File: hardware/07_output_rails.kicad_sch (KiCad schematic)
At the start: 5 parts, among them J2 16-pin IDC POWER OUT, J7 Manual IDC wire landing

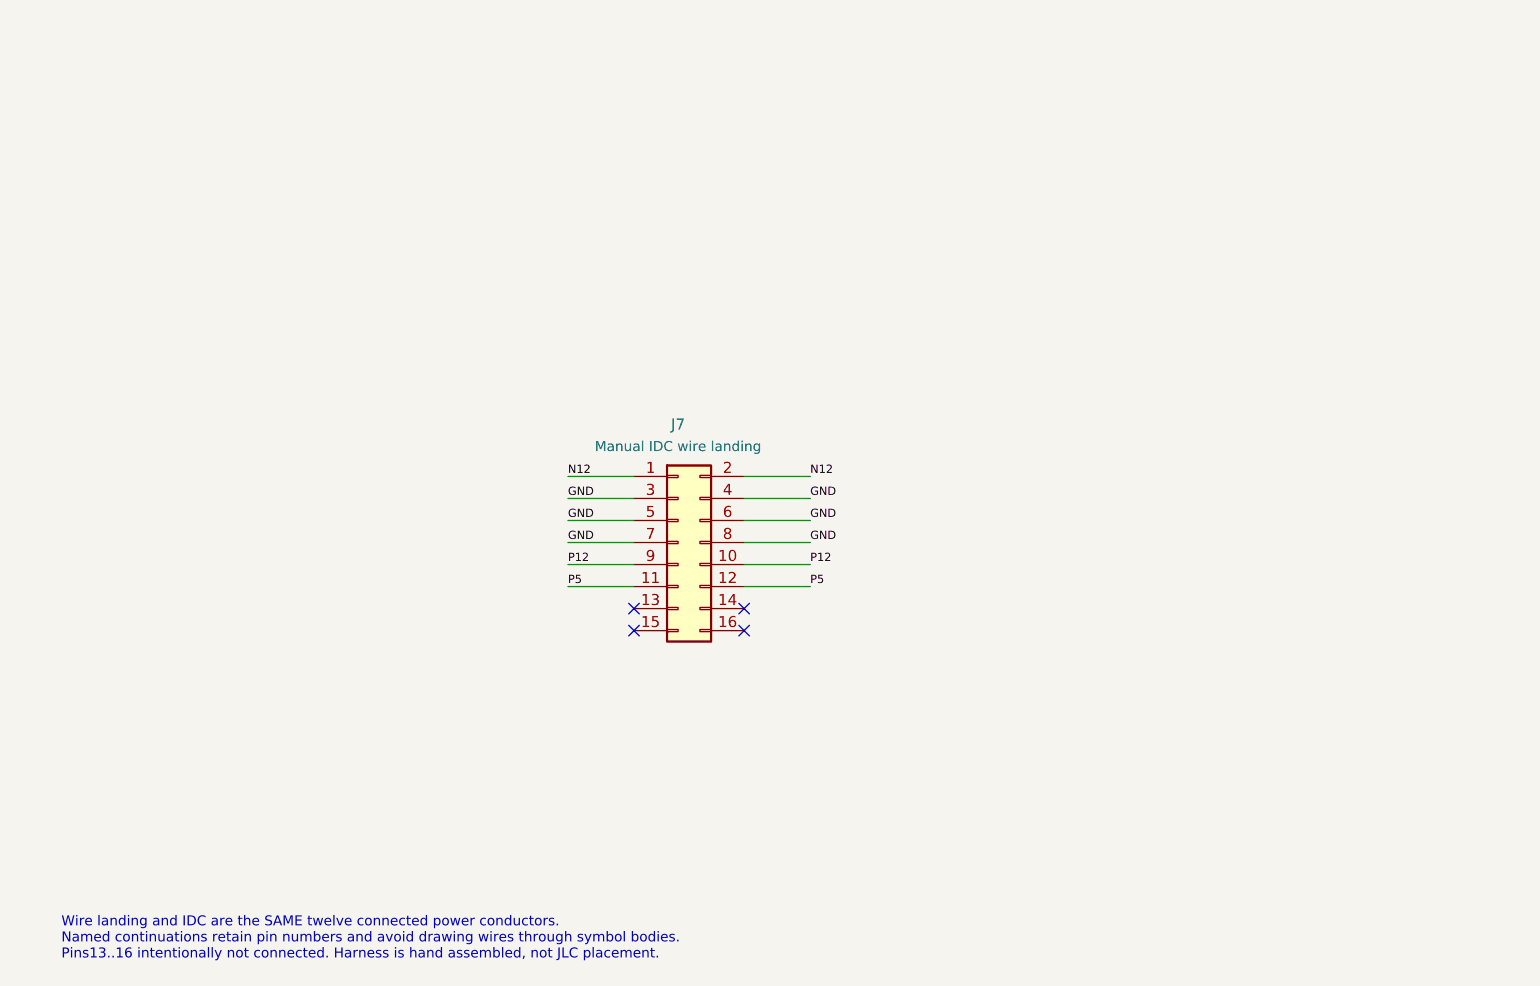
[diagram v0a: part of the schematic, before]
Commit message: Replace MCU diagnostics with optional rail-sense IDC and single 5 V power LED
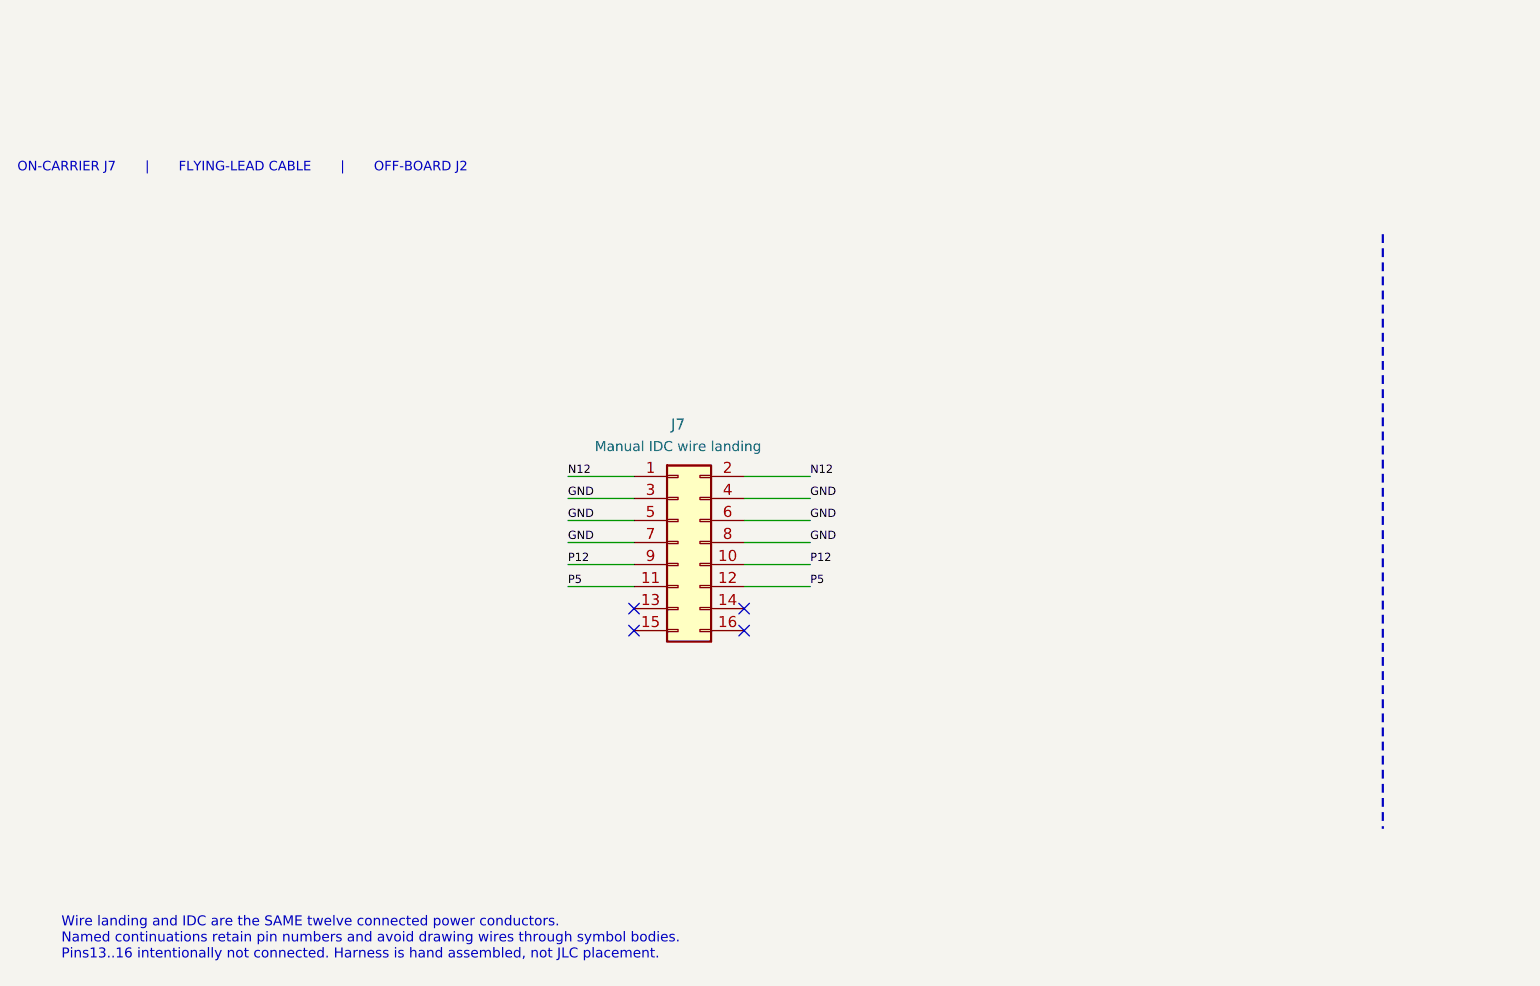
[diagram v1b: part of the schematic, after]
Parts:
- J2: NOTE Off-board cable connector exact MPN open. Manual J7->J2 pin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 -> OFF-BOARD endpoint of ONE J7->J2 flying-lead power harness,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
- J7: NOTE Actual reserved carrier wire landing, not a box header on P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 -> ON-CARRIER numbered solder lands, not an extra purchasable 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
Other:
- note added: "ON-CARRIER J7 | FLYING-LEAD CABLE | OFF-BOARD J2"
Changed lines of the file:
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@@
 (text "07 / MANUAL OUTPUT HARNESS" (at 20.32 17.78 0) (effects (font (size 2.2 2.2)) (justify left)))
 (text "J7 board wire landing -> J2 off-board IDC cable, pin-for-pin.\n1/2=-12, 3..8=GND, 9/10=+12, 11/12=+5; 13..16 NC.\nNever connect another active PSU. Continuity-test red stripe / orientation before use." (at 20.32 30.48 0) (effects (font (size 1.02 1.02)) (justify left)))
+(text "ON-CARRIER J7       |       FLYING-LEAD CABLE       |       OFF-BOARD J2" (at 20.32 60.96 0) (effects (font (size 1.1 1.1)) (justify left)))
+(polyline (pts (xy 177.8 68.58) (xy 177.8 137.16)) (stroke (width 0.254) (type dash)) (fill (type none)))
 (label "N12" (at 83.82 96.52 0) (effects (font (size 0.95 0.95)) (justify left bottom)))
 (label "N12" (at 248.92 96.52 0) (effects (font (size 0.95 0.95)) (justify left bottom)))
@@
 (wire (pts (xy 83.82 238.76) (xy 83.82 243.84)) (stroke (width 0) (type default)))
 (wire (pts (xy 287.02 297.18) (xy 302.26 297.18)) (stroke (width 0) (type default)))
-(symbol (lib_id "BigModular:Connector_Generic_Conn_02x08_Odd_Even") (at 96.52 104.14 0) (unit 1) (in_bom yes) (on_board yes) (dnp no)(property "Reference" "J7" (at 96.52 90.52 0) (effects (font (size 1.27 1.27))))(property "Value" "Manual IDC wire landing" (at 96.52 93.06 0) (effects (font (size 1.15 1.15))))(property "Footprint" "BigModular:WireLanding_2x08_P2.54mm" (at 96.52 104.14 0) (effects (font (size 1 1)) hide))(property "MPN" "" (at 96.52 104.14 0) (effects (font (size 1 1)) hide))(property "LCSC" "" (at 96.52 104.14 0) (effects (font (size 1 1)) hide))(property "NOTE" "Actual reserved carrier wire landing, not a box header on PCB." (at 96.52 104.14 0) (effects (font (size 1 1)) hide))(property "Datasheet" "" (at 96.52 104.14 0) (effects (font (size 1 1)) hide))(property "JLCPCB Exclude" "yes" (at 96.52 104.14 0) (effects (font (size 1 1)) hide))(property "JLCPCB Audit Requirements" "{\"assembly\": \"manual\", \"reason\": \"User-selected manual interface/LED, excluded from JLC placement.\"}" (at 96.52 104.14 0) (effects (font (size 1 1)) hide))(pin "1")(pin "2")(pin "3")(pin "4")(pin "5")(pin "6")(pin "7")(pin "8")(pin "9")(pin "10")(pin "11")(pin "12")(pin "13")(pin "14")(pin "15")(pin "16")(instances (project "big_modular" (path "/d567704c-57ad-5df1-b183-cadb01fd8972/a8d4c238-ef1c-5c41-9eba-d79c1c1014c4" (reference "J7") (unit 1)))) )
-(symbol (lib_id "BigModular:Connector_Generic_Conn_02x08_Odd_Even") (at 261.62 104.14 0) (unit 1) (in_bom yes) (on_board no) (dnp no)(property "Reference" "J2" (at 261.62 90.52 0) (effects (font (size 1.27 1.27))))(property "Value" "16-pin IDC POWER OUT" (at 261.62 93.06 0) (effects (font (size 1.15 1.15))))(property "Footprint" "" (at 261.62 104.14 0) (effects (font (size 1 1)) hide))(property "MPN" "" (at 261.62 104.14 0) (effects (font (size 1 1)) hide))(property "LCSC" "" (at 261.62 104.14 0) (effects (font (size 1 1)) hide))(property "NOTE" "Off-board cable connector exact MPN open. Manual J7->J2 pin-for-pin, red stripe pins1/2." (at 261.62 104.14 0) (effects (font (size 1 1)) hide))(property "Datasheet" "" (at 261.62 104.14 0) (effects (font (size 1 1)) hide))(property "JLCPCB Exclude" "yes" (at 261.62 104.14 0) (effects (font (size 1 1)) hide))(property "JLCPCB Audit Requirements" "{\"assembly\": \"manual\", \"reason\": \"User-selected manual interface/LED, excluded from JLC placement.\"}" (at 261.62 104.14 0) (effects (font (size 1 1)) hide))(pin "1")(pin "2")(pin "3")(pin "4")(pin "5")(pin "6")(pin "7")(pin "8")(pin "9")(pin "10")(pin "11")(pin "12")(pin "13")(pin "14")(pin "15")(pin "16")(instances (project "big_modular" (path "/d567704c-57ad-5df1-b183-cadb01fd8972/a8d4c238-ef1c-5c41-9eba-d79c1c1014c4" (reference "J2") (unit 1)))) )
+(symbol (lib_id "BigModular:Connector_Generic_Conn_02x08_Odd_Even") (at 96.52 104.14 0) (unit 1) (in_bom yes) (on_board yes) (dnp no)(property "Reference" "J7" (at 96.52 90.52 0) (effects (font (size 1.27 1.27))))(property "Value" "Manual IDC wire landing" (at 96.52 93.06 0) (effects (font (size 1.15 1.15))))(property "Footprint" "BigModular:WireLanding_2x08_P2.54mm" (at 96.52 104.14 0) (effects (font (size 1 1)) hide))(property "MPN" "" (at 96.52 104.14 0) (effects (font (size 1 1)) hide))(property "LCSC" "" (at 96.52 104.14 0) (effects (font (size 1 1)) hide))(property "NOTE" "ON-CARRIER numbered solder lands, not an extra purchasable box header. Physical cable boundary to off-board J2; one power output harness, not two sources. NOT debug J8." (at 96.52 104.14 0) (effects (font (size 1 1)) hide))(property "Datasheet" "" (at 96.52 104.14 0) (effects (font (size 1 1)) hide))(property "JLCPCB Exclude" "yes" (at 96.52 104.14 0) (effects (font (size 1 1)) hide))(property "JLCPCB Audit Requirements" "{\"assembly\": \"manual\", \"reason\": \"User-selected manual interface/LED, excluded from JLC placement.\"}" (at 96.52 104.14 0) (effects (font (size 1 1)) hide))(pin "1")(pin "2")(pin "3")(pin "4")(pin "5")(pin "6")(pin "7")(pin "8")(pin "9")(pin "10")(pin "11")(pin "12")(pin "13")(pin "14")(pin "15")(pin "16")(instances (project "big_modular" (path "/d567704c-57ad-5df1-b183-cadb01fd8972/a8d4c238-ef1c-5c41-9eba-d79c1c1014c4" (reference "J7") (unit 1)))) )
+(symbol (lib_id "BigModular:Connector_Generic_Conn_02x08_Odd_Even") (at 261.62 104.14 0) (unit 1) (in_bom yes) (on_board no) (dnp no)(property "Reference" "J2" (at 261.62 90.52 0) (effects (font (size 1.27 1.27))))(property "Value" "16-pin IDC POWER OUT" (at 261.62 93.06 0) (effects (font (size 1.15 1.15))))(property "Footprint" "" (at 261.62 104.14 0) (effects (font (size 1 1)) hide))(property "MPN" "" (at 261.62 104.14 0) (effects (font (size 1 1)) hide))(property "LCSC" "" (at 261.62 104.14 0) (effects (font (size 1 1)) hide))(property "NOTE" "OFF-BOARD endpoint of ONE J7->J2 flying-lead power harness, not a second active output. Exact keyed male MPN open; manual harness assembly includes J2 once, no PCB/JLC placement. Red stripe pins1/2=-12V. NOT debug J8." (at 261.62 104.14 0) (effects (font (size 1 1)) hide))(property "Datasheet" "" (at 261.62 104.14 0) (effects (font (size 1 1)) hide))(property "JLCPCB Exclude" "yes" (at 261.62 104.14 0) (effects (font (size 1 1)) hide))(property "JLCPCB Audit Requirements" "{\"assembly\": \"manual\", \"reason\": \"User-selected manual interface/LED, excluded from JLC placement.\"}" (at 261.62 104.14 0) (effects (font (size 1 1)) hide))(pin "1")(pin "2")(pin "3")(pin "4")(pin "5")(pin "6")(pin "7")(pin "8")(pin "9")(pin "10")(pin "11")(pin "12")(pin "13")(pin "14")(pin "15")(pin "16")(instances (project "big_modular" (path "/d567704c-57ad-5df1-b183-cadb01fd8972/a8d4c238-ef1c-5c41-9eba-d79c1c1014c4" (reference "J2") (unit 1)))) )
 (symbol (lib_id "BigModular:Device_R") (at 63.5 193.04 0) (unit 1) (in_bom yes) (on_board yes) (dnp no)(property "Reference" "R25" (at 66.5 191.84 0) (effects (font (size 1.27 1.27)) (justify left)))(property "Value" "10k 1%" (at 66.5 194.38 0) (effects (font (size 1.15 1.15)) (justify left)))(property "Footprint" "BigModular:R_0603_1608Metric" (at 63.5 193.04 0) (effects (font (size 1 1)) hide))(property "MPN" "0603WAF1002T5E" (at 63.5 193.04 0) (effects (font (size 1 1)) hide))(property "LCSC" "C25804" (at 63.5 193.04 0) (effects (font (size 1 1)) hide))(property "NOTE" "Bleed provision only; does not prove rail discharge time or prevent backfeed." (at 63.5 193.04 0) (effects (font (size 1 1)) hide))(property "Datasheet" "" (at 63.5 193.04 0) (effects (font (size 1 1)) hide))(property "JLCPCB Exclude" "no" (at 63.5 193.04 0) (effects (font (size 1 1)) hide))(property "JLCPCB Audit Requirements" "{}" (at 63.5 193.04 0) (effects (font (size 1 1)) hide))(pin "1")(pin "2")(instances (project "big_modular" (path "/d567704c-57ad-5df1-b183-cadb01fd8972/a8d4c238-ef1c-5c41-9eba-d79c1c1014c4" (reference "R25") (unit 1)))) )
 (symbol (lib_id "BigModular:Device_R") (at 132.08 193.04 0) (unit 1) (in_bom yes) (on_board yes) (dnp no)(property "Reference" "R26" (at 135.08 191.84 0) (effects (font (size 1.27 1.27)) (justify left)))(property "Value" "10k 1%" (at 135.08 194.38 0) (effects (font (size 1.15 1.15)) (justify left)))(property "Footprint" "BigModular:R_0603_1608Metric" (at 132.08 193.04 0) (effects (font (size 1 1)) hide))(property "MPN" "0603WAF1002T5E" (at 132.08 193.04 0) (effects (font (size 1 1)) hide))(property "LCSC" "C25804" (at 132.08 193.04 0) (effects (font (size 1 1)) hide))(property "NOTE" "Bleed provision only; does not prove rail discharge time or prevent backfeed." (at 132.08 193.04 0) (effects (font (size 1 1)) hide))(property "Datasheet" "" (at 132.08 193.04 0) (effects (font (size 1 1)) hide))(property "JLCPCB Exclude" "no" (at 132.08 193.04 0) (effects (font (size 1 1)) hide))(property "JLCPCB Audit Requirements" "{}" (at 132.08 193.04 0) (effects (font (size 1 1)) hide))(pin "1")(pin "2")(instances (project "big_modular" (path "/d567704c-57ad-5df1-b183-cadb01fd8972/a8d4c238-ef1c-5c41-9eba-d79c1c1014c4" (reference "R26") (unit 1)))) )
